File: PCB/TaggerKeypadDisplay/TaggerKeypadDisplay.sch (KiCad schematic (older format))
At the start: 2 parts

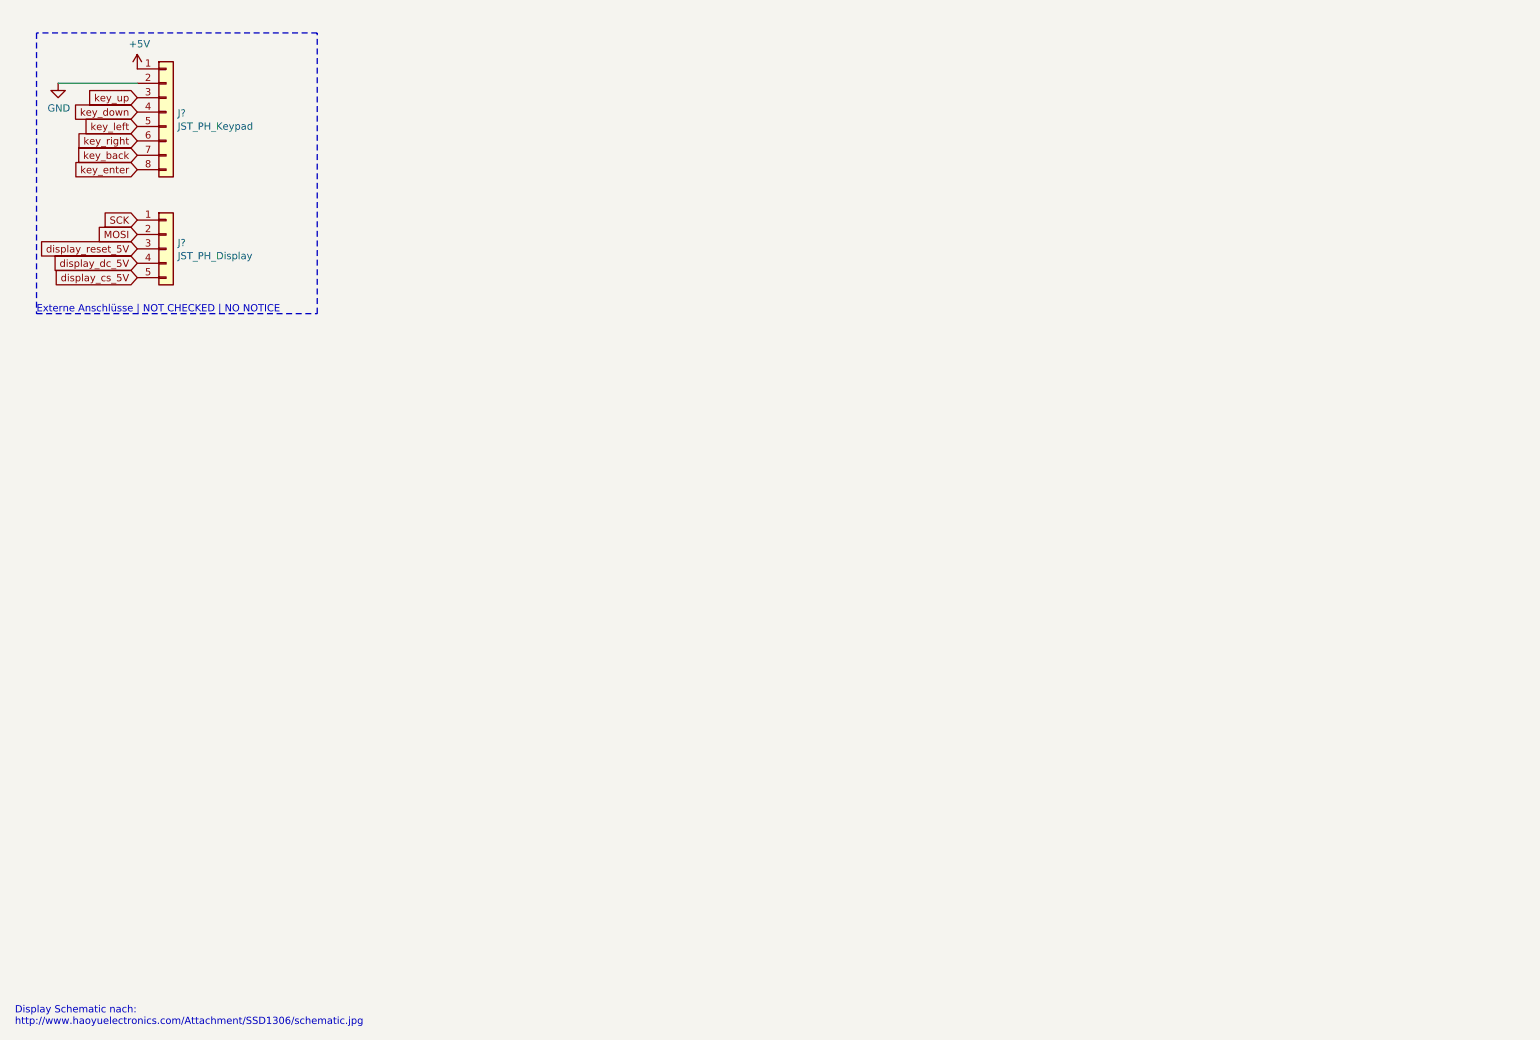
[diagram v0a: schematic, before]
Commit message: Keypad + Bohrungen + Logo & Co
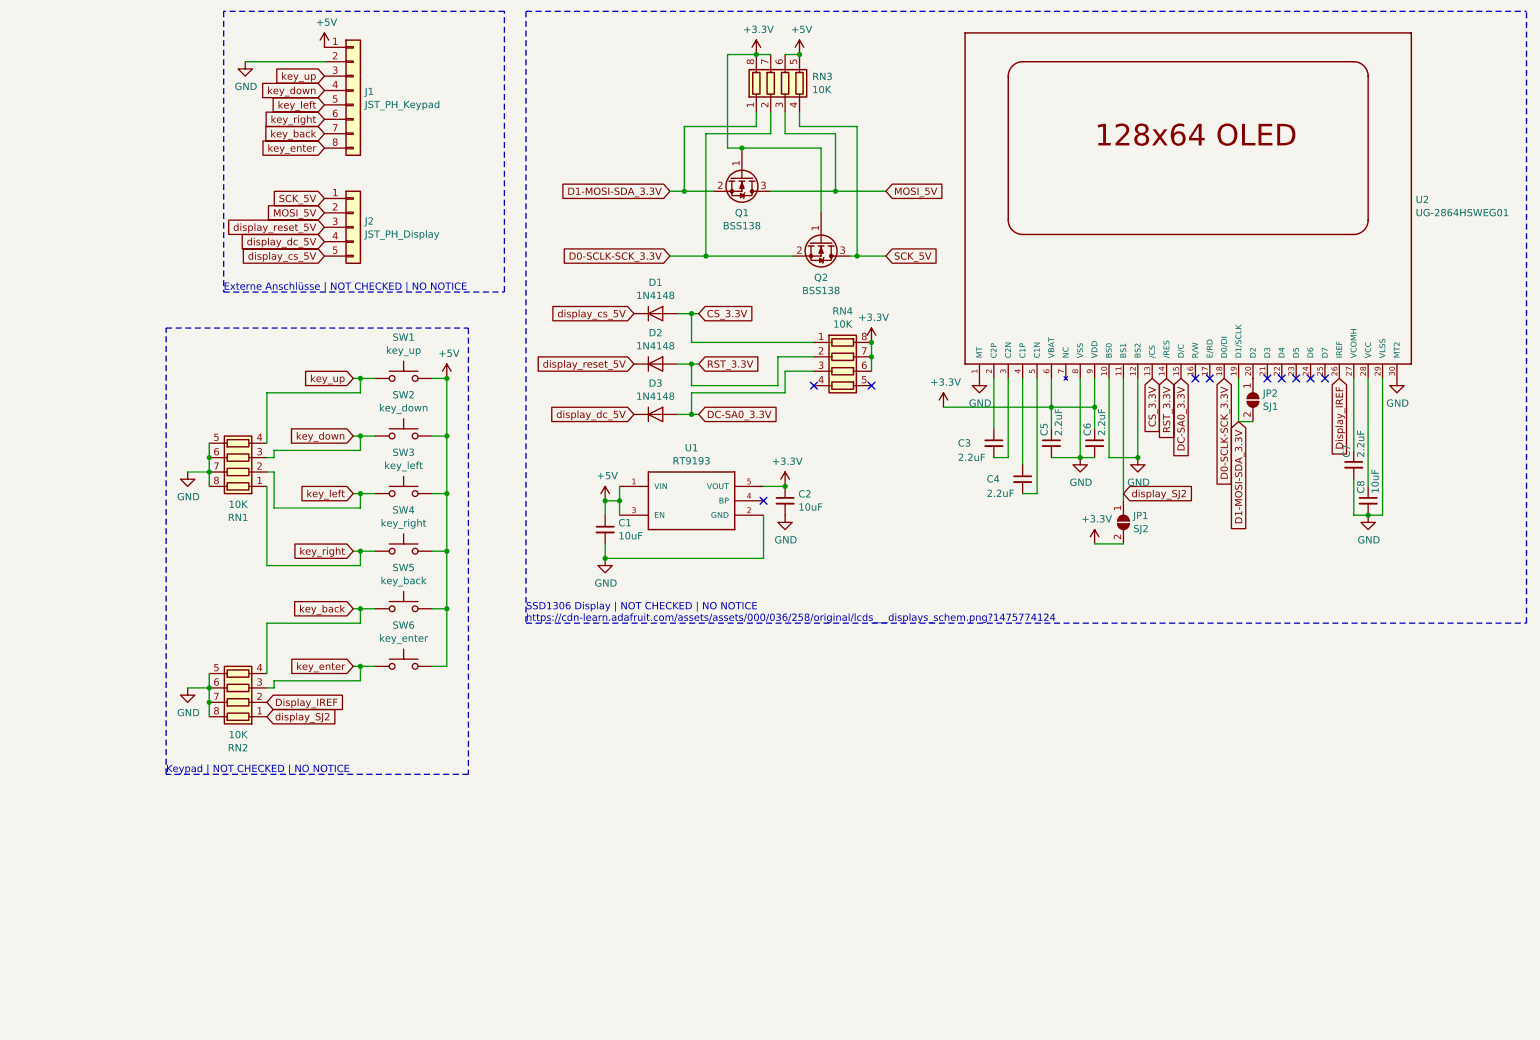
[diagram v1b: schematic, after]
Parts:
- added C1, C2, C8: 10uF, Capacitor_SMD:C_0805_2012Metric, symbol Device:C_Small
- added C3, C4, C5, C6, C7: 2.2uF, Capacitor_SMD:C_0805_2012Metric, symbol Device:C_Small
- added D1, D2, D3: 1N4148, Diode_SMD:D_0805_2012Metric, symbol Diode:1N4148
- added JP1: SJ2, Jumper:SolderJumper-2_P1.3mm_Open_Pad1.0x1.5mm, symbol Jumper:SolderJumper_2_Open
- added JP2: SJ1, Jumper:SolderJumper-2_P1.3mm_Open_Pad1.0x1.5mm, symbol Jumper:SolderJumper_2_Open
- added Q1, Q2: BSS138, Package_TO_SOT_SMD:SOT-23, symbol Transistor_FET:BSS138
- added RN1, RN2, RN3, RN4: 10K, Resistor_SMD:R_Array_Convex_4x0603, symbol Device:R_Pack04
- added SW1: key_up, Infinitag:Infinitag_Keypad_Button, symbol Switch:SW_Push
- added SW2: key_down, Infinitag:Infinitag_Keypad_Button, symbol Switch:SW_Push
- added SW3: key_left, Infinitag:Infinitag_Keypad_Button, symbol Switch:SW_Push
- added SW4: key_right, Infinitag:Infinitag_Keypad_Button, symbol Switch:SW_Push
- added SW5: key_back, Infinitag:Infinitag_Keypad_Button, symbol Switch:SW_Push
- added SW6: key_enter, Infinitag:Infinitag_Keypad_Button, symbol Switch:SW_Push
- added U1: RT9193, RT9193-33GB:SOT94P279X129-5N, symbol RT9193-33GB:RT9193-33GB
- added U2: UG-2864HSWEG01, UG-2864HSWEG01:1X30-0.7MM, symbol UG-2864HSWEG01:UG-2864HSWEG01
- J1: renamed from J?; footprint (none) -> Connector_JST:JST_PH_B8B-PH-K_1x08_P2.00mm_Vertical
- J2: renamed from J?; footprint (none) -> Connector_JST:JST_PH_B5B-PH-K_1x05_P2.00mm_Vertical
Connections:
- net +5V: now also C1.1, RN3.5 (R4.2), RN3.6 (R3.2), SW1.2, SW2.2, SW3.2, SW4.2, SW5.2, SW6.2, U1.1 (VIN), U1.3 (EN)
- net GND: now also C1.2, C2.2, C5.2, C6.2, C7.2, C8.2, RN1.5 (R4.2), RN1.6 (R3.2), RN1.7 (R2.2), RN1.8 (R1.2), RN2.5 (R4.2), RN2.6 (R3.2), RN2.7 (R2.2), RN2.8 (R1.2), U1.2 (GND), U2.1 (MT), U2.10 (BS0), U2.12 (BS2), U2.29 (VLSS), U2.30 (MT2), U2.8 (VSS)
- net display_cs_5V: now also D1.1 (K)
- net display_dc_5V: now also D3.1 (K)
- net display_reset_5V: now also D2.1 (K)
- net key_back: now also RN2.4 (R4.1), SW5.1
- net key_down: now also RN1.3 (R3.1), SW2.1
- net key_enter: now also RN2.3 (R3.1), SW6.1
- net key_left: now also RN1.2 (R2.1), SW3.1
- net key_right: now also RN1.1 (R1.1), SW4.1
- net key_up: now also RN1.4 (R4.1), SW1.1
- net MOSI renamed MOSI_5V
- net MOSI_5V: now also Q1.3 (D), RN3.3 (R3.1)
- net SCK renamed SCK_5V
- net SCK_5V: now also Q2.3 (D), RN3.4 (R4.1)
- new net: C3.1, U2.2 (C2P)
- new net: JP2.1 (A), U2.20 (D2)
- new net: C7.1, U2.27 (VCOMH)
- new net: C8.1, U2.28 (VCC)
- new net: C3.2, U2.3 (C2N)
- new net: C4.1, U2.4 (C1P)
- new net: C4.2, U2.5 (C1N)
- new net +3V3: C2.1, C5.1, C6.1, JP1.2 (B), Q1.1 (G), Q2.1 (G), RN3.7 (R2.2), RN3.8 (R1.2), RN4.6 (R3.2), RN4.7 (R2.2), RN4.8 (R1.2), U1.5 (VOUT), U2.6 (VBAT), U2.9 (VDD)
- new net CS_3.3V: D1.2 (A), RN4.1 (R1.1), U2.13 (/CS)
- new net D0-SCLK-SCK_3.3V: Q2.2 (S), RN3.2 (R2.1), U2.18 (D0/DI)
- new net D1-MOSI-SDA_3.3V: JP2.2 (B), Q1.2 (S), RN3.1 (R1.1), U2.19 (D1/SCLK)
- new net DC-SA0_3.3V: D3.2 (A), RN4.3 (R3.1), U2.15 (D/C)
- new net Display_IREF: RN2.2 (R2.1), U2.26 (IREF)
- new net RST_3.3V: D2.2 (A), RN4.2 (R2.1), U2.14 (/RES)
- new net display_SJ2: JP1.1 (A), RN2.1 (R1.1), U2.11 (BS1)
- no-connect marks 0 -> 10
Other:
- note added: "Keypad | NOT CHECKED | NO NOTICE"
- note added: "SSD1306 Display | NOT CHECKED | NO NOTICE\nhttps://cdn-learn.adafruit.com/assets/assets/000/036/258/original/lcds___displays_schem.png?1475774124"
- note removed: "Display Schematic nach: \nhttp://www.haoyuelectronics.com/Attachment/SSD1306/schematic.jpg"
- moved on the sheet: J1, J2

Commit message: Anpassungen
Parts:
- D1, D2, D3: footprint Diode_SMD:D_0805_2012Metric -> Diode_SMD:D_SOD-123
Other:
- note added: "ToDo\n====================================\n[ ] Display-Anschluss zu weit entfernt"
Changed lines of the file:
@@
 F 0 "D1" H 5050 2916 50  0000 C CNN
 F 1 "1N4148" H 5050 2825 50  0000 C CNN
-F 2 "Diode_SMD:D_0805_2012Metric" H 5050 2525 50  0001 C CNN
+F 2 "Diode_SMD:D_SOD-123" H 5050 2525 50  0001 C CNN
 F 3 "http://www.nxp.com/documents/data_sheet/1N4148_1N4448.pdf" H 5050 2700 50  0001 C CNN
 	1    5050 2700
@@
 F 0 "D2" H 5050 3266 50  0000 C CNN
 F 1 "1N4148" H 5050 3175 50  0000 C CNN
-F 2 "Diode_SMD:D_0805_2012Metric" H 5050 2875 50  0001 C CNN
+F 2 "Diode_SMD:D_SOD-123" H 5050 2875 50  0001 C CNN
 F 3 "http://www.nxp.com/documents/data_sheet/1N4148_1N4448.pdf" H 5050 3050 50  0001 C CNN
 	1    5050 3050
@@
 F 0 "D3" H 5050 3616 50  0000 C CNN
 F 1 "1N4148" H 5050 3525 50  0000 C CNN
-F 2 "Diode_SMD:D_0805_2012Metric" H 5050 3225 50  0001 C CNN
+F 2 "Diode_SMD:D_SOD-123" H 5050 3225 50  0001 C CNN
 F 3 "http://www.nxp.com/documents/data_sheet/1N4148_1N4448.pdf" H 5050 3400 50  0001 C CNN
 	1    5050 3400
@@
 Text GLabel 2350 5500 2    50   Input ~ 0
 display_SJ2
+Text Notes 7050 5800 0    50   ~ 0
+ToDo\n====================================\n[  ] Display-Anschluss zu weit entfernt
 $EndSCHEMATC
